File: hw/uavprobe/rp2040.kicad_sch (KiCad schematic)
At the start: 44 parts, among them IC1 UCLAMP3306P.TCT, SW1 Boot, U1 W25Q16JVSS, U2 NCP1117-5.0_SOT223, U3 RP2040, U4 TJA1051T-3, U5 TJA1051T-3, Y1 ABLS-12.000MHZ-B4-T

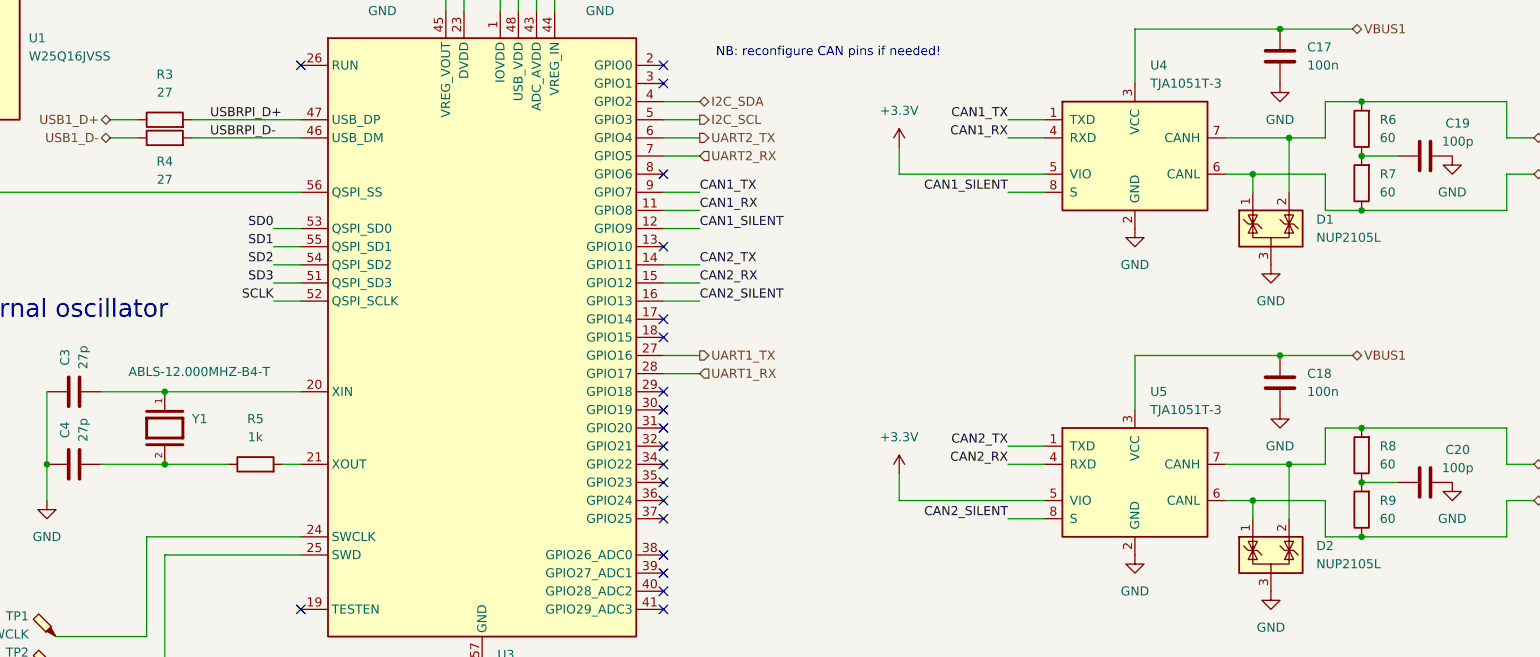
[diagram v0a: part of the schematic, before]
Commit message: AISLER-friendly BOM fields
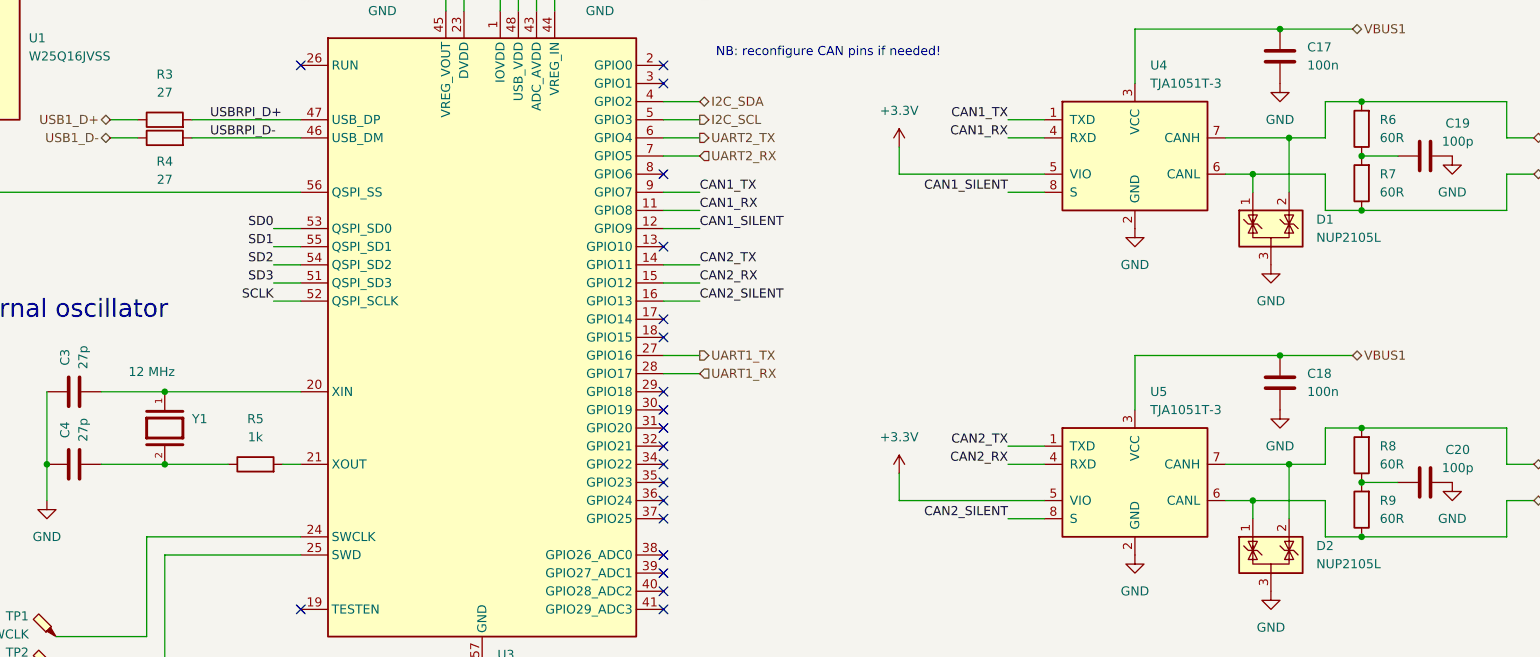
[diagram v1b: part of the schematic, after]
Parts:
- R6, R7, R8, R9: value 60 -> 60R
- SW1: MPN SW_SPST_B3U-1000P -> B3U-1000PM
- TP1, TP2, TP3, TP4, TP5: now left out of the parts list
- U1: MPN W25Q16JVSS -> W25Q16JVSSIQ
- U2: MPN NCP1117-5.0_SOT223 -> NCP1117ST33T3G
- U3: MPN SC0914 -> SC0914(7)
- U4, U5: MPN TJA1051T-3 -> TJA1051T/3/1J
- Y1: value ABLS-12.000MHZ-B4-T -> 12 MHz
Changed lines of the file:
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@@
 		(unit 1)
 		(exclude_from_sim no)
-		(in_bom yes)
+		(in_bom no)
 		(on_board yes)
 		(dnp no)
@@
 		(unit 1)
 		(exclude_from_sim no)
-		(in_bom yes)
+		(in_bom no)
 		(on_board yes)
 		(dnp no)
@@
 			)
 		)
-		(property "Value" "60"
+		(property "Value" "60R"
 			(at 248.92 99.0599 0)
 			(effects
@@
 			)
 		)
-		(property "Value" "ABLS-12.000MHZ-B4-T"
+		(property "Value" "12 MHz"
 			(at 73.66 124.206 90)
 			(effects
@@
 		(unit 1)
 		(exclude_from_sim no)
-		(in_bom yes)
+		(in_bom no)
 		(on_board yes)
 		(dnp no)
@@
 			)
 		)
-		(property "MPN" "NCP1117-5.0_SOT223"
+		(property "MPN" "NCP1117ST33T3G"
 			(at 83.82 27.94 0)
 			(effects
@@
 		(unit 1)
 		(exclude_from_sim no)
-		(in_bom yes)
+		(in_bom no)
 		(on_board yes)
 		(dnp no)
@@
 			)
 		)
-		(property "MPN" "TJA1051T-3"
+		(property "MPN" "TJA1051T/3/1J "
 			(at 214.63 93.98 0)
 			(effects
@@
 			)
 		)
-		(property "Value" "60"
+		(property "Value" "60R"
 			(at 248.92 91.4399 0)
 			(effects
@@
 			)
 		)
-		(property "MPN" "SC0914"
+		(property "MPN" "SC0914(7)"
 			(at 123.19 119.38 0)
 			(effects
@@
 			)
 		)
-		(property "MPN" "W25Q16JVSS"
+		(property "MPN" "W25Q16JVSSIQ"
 			(at 48.26 78.74 0)
 			(effects
@@
 			)
 		)
-		(property "Value" "60"
+		(property "Value" "60R"
 			(at 248.92 137.1599 0)
 			(effects
@@
 			)
 		)
-		(property "Value" "60"
+		(property "Value" "60R"
 			(at 248.92 144.7799 0)
 			(effects
@@
 		(unit 1)
 		(exclude_from_sim no)
-		(in_bom yes)
+		(in_bom no)
 		(on_board yes)
 		(dnp no)
@@
 			)
 		)
-		(property "MPN" "SW_SPST_B3U-1000P"
+		(property "MPN" "B3U-1000PM"
 			(at 25.4 130.81 90)
 			(effects
@@
 			)
 		)
-		(property "MPN" "TJA1051T-3"
+		(property "MPN" "TJA1051T/3/1J"
 			(at 214.63 139.7 0)
 			(effects

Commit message: Layout 2
Honoring the DRC and with a new uSB-C connector
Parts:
- U3: footprint Package_DFN_QFN:QFN-56-1EP_7x7mm_P0.4mm_EP3.2x3.2mm -> Package_DFN_QFN:QFN-56-1EP_7x7mm_P0.4mm_EP3.2x3.2mm_ThermalVias
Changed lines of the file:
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@@
 			)
 		)
-		(property "Footprint" "Package_DFN_QFN:QFN-56-1EP_7x7mm_P0.4mm_EP3.2x3.2mm"
+		(property "Footprint" "Package_DFN_QFN:QFN-56-1EP_7x7mm_P0.4mm_EP3.2x3.2mm_ThermalVias"
 			(at 123.19 119.38 0)
 			(effects
